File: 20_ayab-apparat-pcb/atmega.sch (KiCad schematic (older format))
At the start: 15 parts

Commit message: Switched to ATmega32u4 Added USB Connector and external Caps
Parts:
- removed IC?: ATMEGA328-M, MLF/QFN32, symbol ATMEGA328-M
- added C? (x6): C, symbol C
- added CON?: USB-MINI-B, symbol USB-MINI-B
- added D? (x2): LED, symbol LED
- added F?: FUSE, symbol FUSE
- added L? (x2): INDUCTOR, symbol INDUCTOR
- added R? (x4): R, symbol R
- added U?: ATMEGA32U4-A, TQFP44, symbol ATMEGA32U4-A
- added VR? (x2): VR, symbol VR
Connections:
- net labels added: AVCC, D+, D-, EOL_L, EOL_R, RD+, RD-, RXLED, TXLED, UCAP, UGND, USBID, VUSB
- net labels removed: SER_RX, SER_TX
- wire segments 59 -> 124
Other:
- note added: "TODO Check 5V Power Supply (from USB? from Machine?)\nTODO Add Debug LEDs\nTODO Add 5V/GND/I2C Connector for extensions\nTODO Add Beeper Connector"
- moved on the sheet: C?, R?

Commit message: schematic structure finished -> todo add part values
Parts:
- removed C? (x2): C, symbol C
- removed CON?: USB-MINI-B, symbol USB-MINI-B
- removed L? (x2): INDUCTOR, symbol INDUCTOR
- added C?: CAPAPOL, symbol CAPAPOL
- added D? (x2): LED, symbol LED
- added P?: CONN_2, symbol CONN_2
- added P?: CONN_4, symbol CONN_4
- added R? (x2): R, symbol R
- added U? (x2): FERRITE, symbol FERRITE
- added X?: USBMICRO, symbol USBMICRO
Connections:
- net labels added: BEEPER, LED1, LED2
- net labels removed: USBID
- wire segments 124 -> 161
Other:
- note added: "I2C Pullups"
- note added: "License : CC BY-SA\nhttp://creativecommons.org/licenses/by-sa/3.0/\n\nBased on Arduino Leonardo design from http://arduino.cc"
- note removed: "TODO Check 5V Power Supply (from USB? from Machine?)\nTODO Add Debug LEDs\nTODO Add 5V/GND/I2C Connector for extensions\nTODO Add Beeper Connector"
- moved on the sheet: C?, D?, F?, P?, R?, SW?, U?, VR?, X?

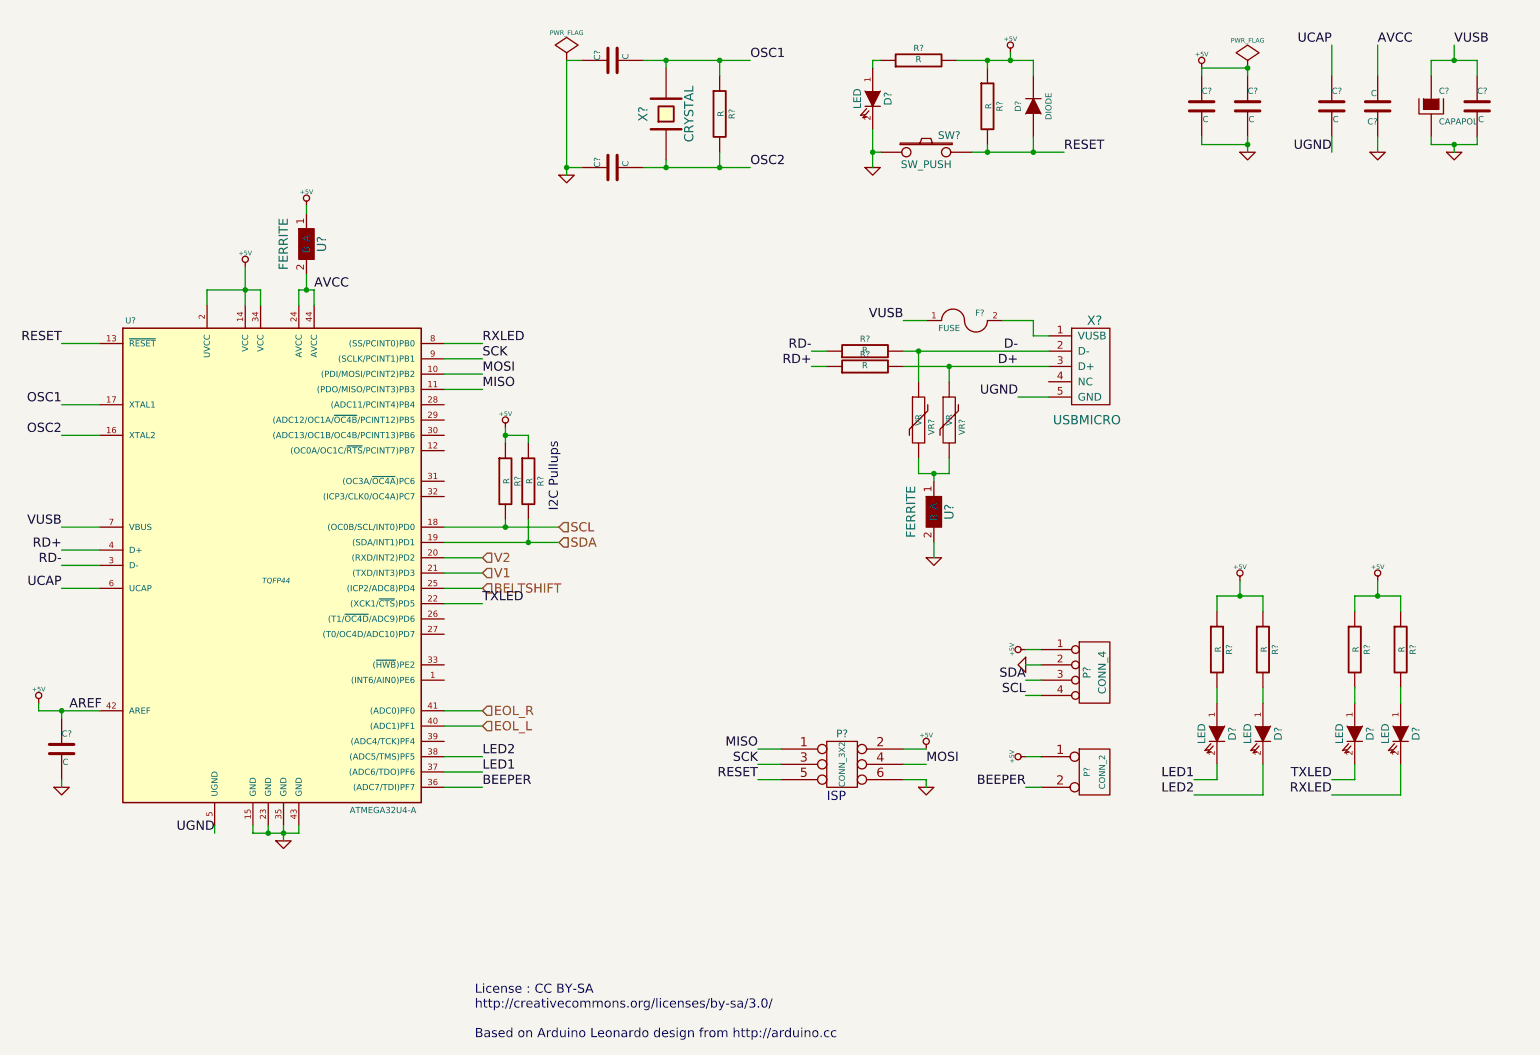
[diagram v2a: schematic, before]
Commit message: added partnames and values, generated first version of netlist, ready to assign footprints
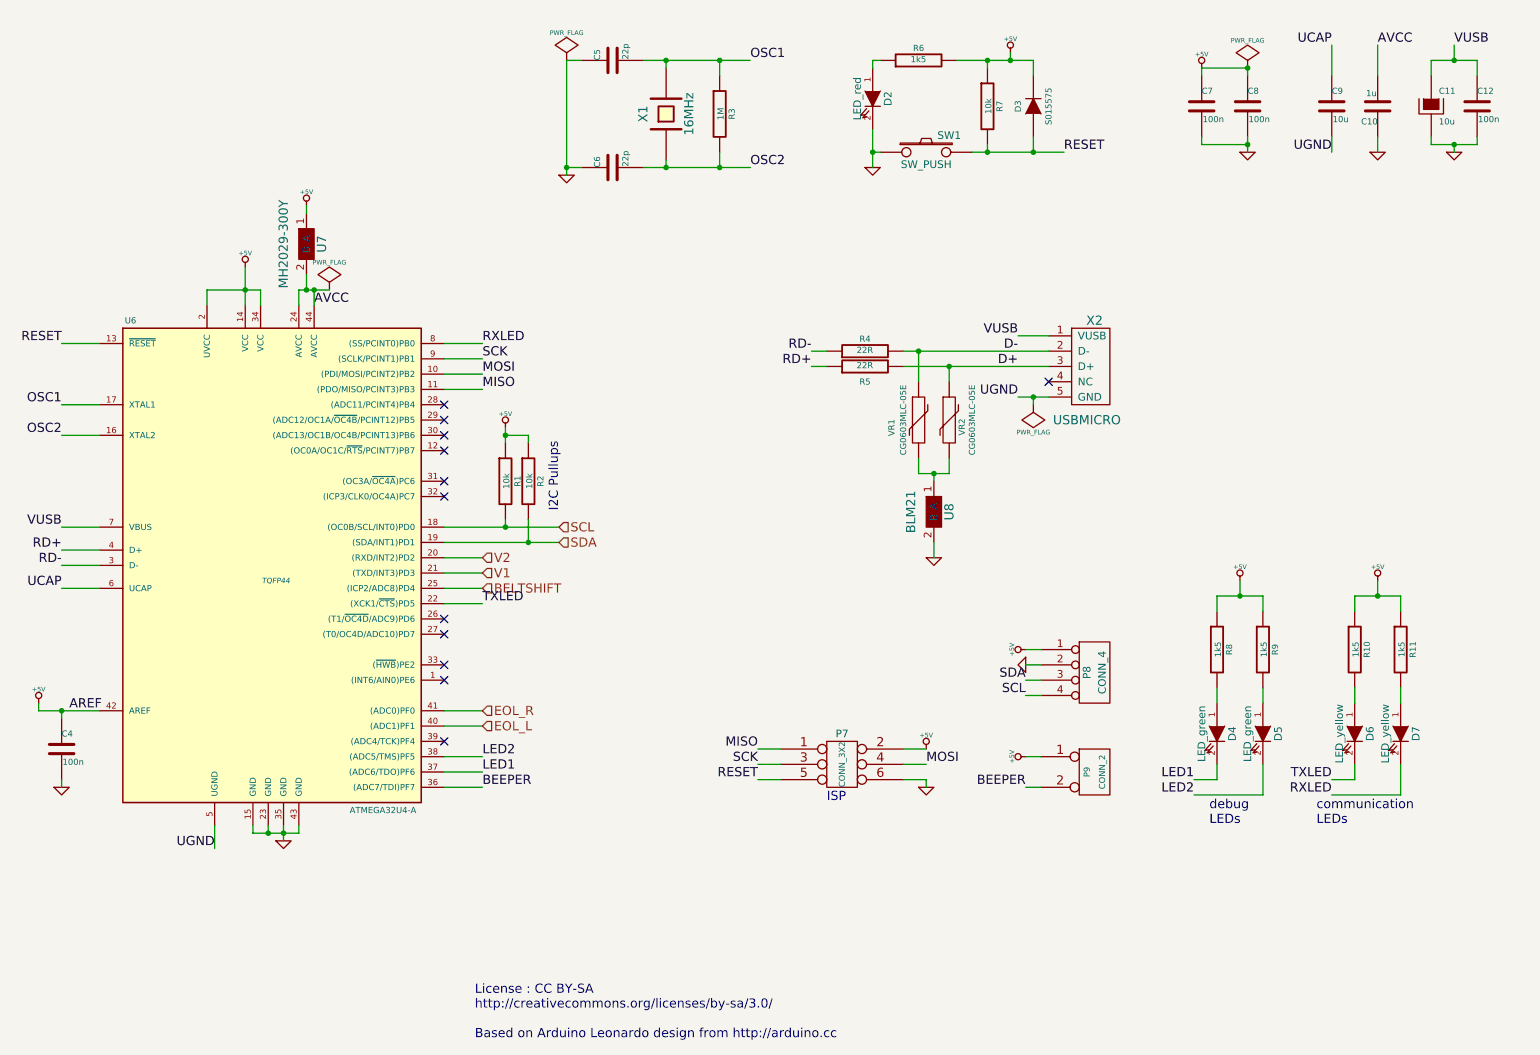
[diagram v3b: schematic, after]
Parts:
- removed F?: FUSE, symbol FUSE
- C10: renamed from C?; value C -> 1u
- C11: renamed from C?; value CAPAPOL -> 10u
- C12, C4, C7, C8: renamed from C?; value C -> 100n
- C5, C6: renamed from C?; value C -> 22p
- C9: renamed from C?; value C -> 10u
- D2: renamed from D?; value LED -> LED_red
- D3: renamed from D?; value DIODE -> S015575
- D4, D5: renamed from D?; value LED -> LED_green
- D6, D7: renamed from D?; value LED -> LED_yellow
- R1, R2, R7: renamed from R?; value R -> 10k
- R10, R11, R6, R8, R9: renamed from R?; value R -> 1k5
- R3: renamed from R?; value R -> 1M
- R4, R5: renamed from R?; value R -> 22R
- U7: renamed from U?; value FERRITE -> MH2029-300Y
- U8: renamed from U?; value FERRITE -> BLM21
- VR1, VR2: renamed from VR?; value VR -> CG0603MLC-05E
- X1: renamed from X?; value CRYSTAL -> 16MHz
- gave numbers to parts that had none: 6
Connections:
- net VUSB: now also X2.1 (VUSB)
- no-connect marks 0 -> 12
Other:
- note added: "communication\nLEDs"
- note added: "debug\nLEDs"

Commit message: Added Packages and minor changes in schematic
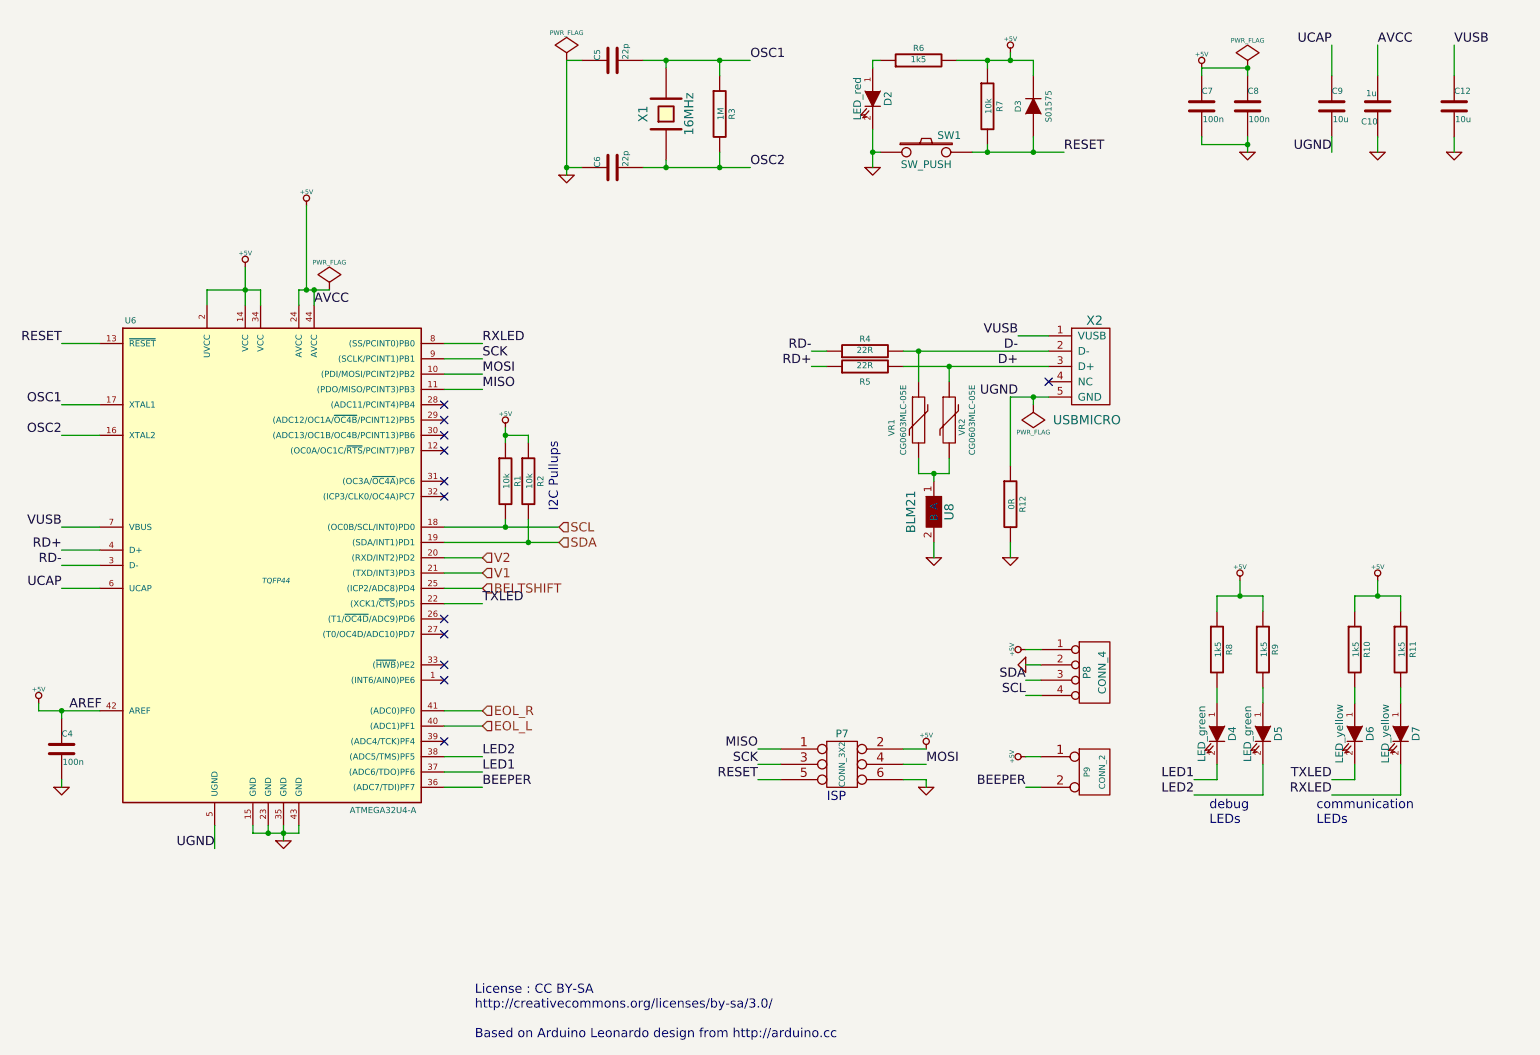
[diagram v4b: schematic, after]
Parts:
- removed C11: 10u, symbol CAPAPOL
- removed U7: MH2029-300Y, symbol FERRITE
- added R12: 0R, symbol R
- C12: value 100n -> 10u
- D3: value S015575 -> S01575
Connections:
- net AVCC is gone; now on net +5V: C10.2, U6.24 (AVCC), U6.44 (AVCC)
- net GND: now also R12.2
- net UGND: now also R12.1
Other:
- moved on the sheet: C12
